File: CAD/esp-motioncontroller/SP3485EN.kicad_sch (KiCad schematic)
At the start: 54 parts, among them J2 Screw_Terminal_01x10, J3 Screw_Terminal_01x10, J4 Screw_Terminal_01x10, J5 Screw_Terminal_01x03, J6 Screw_Terminal_01x10, J8 Screw_Terminal_01x10, U10 AM26LS31CDR, U11 LTV-817S, U12 LTV-817S, U13 LTV-817S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

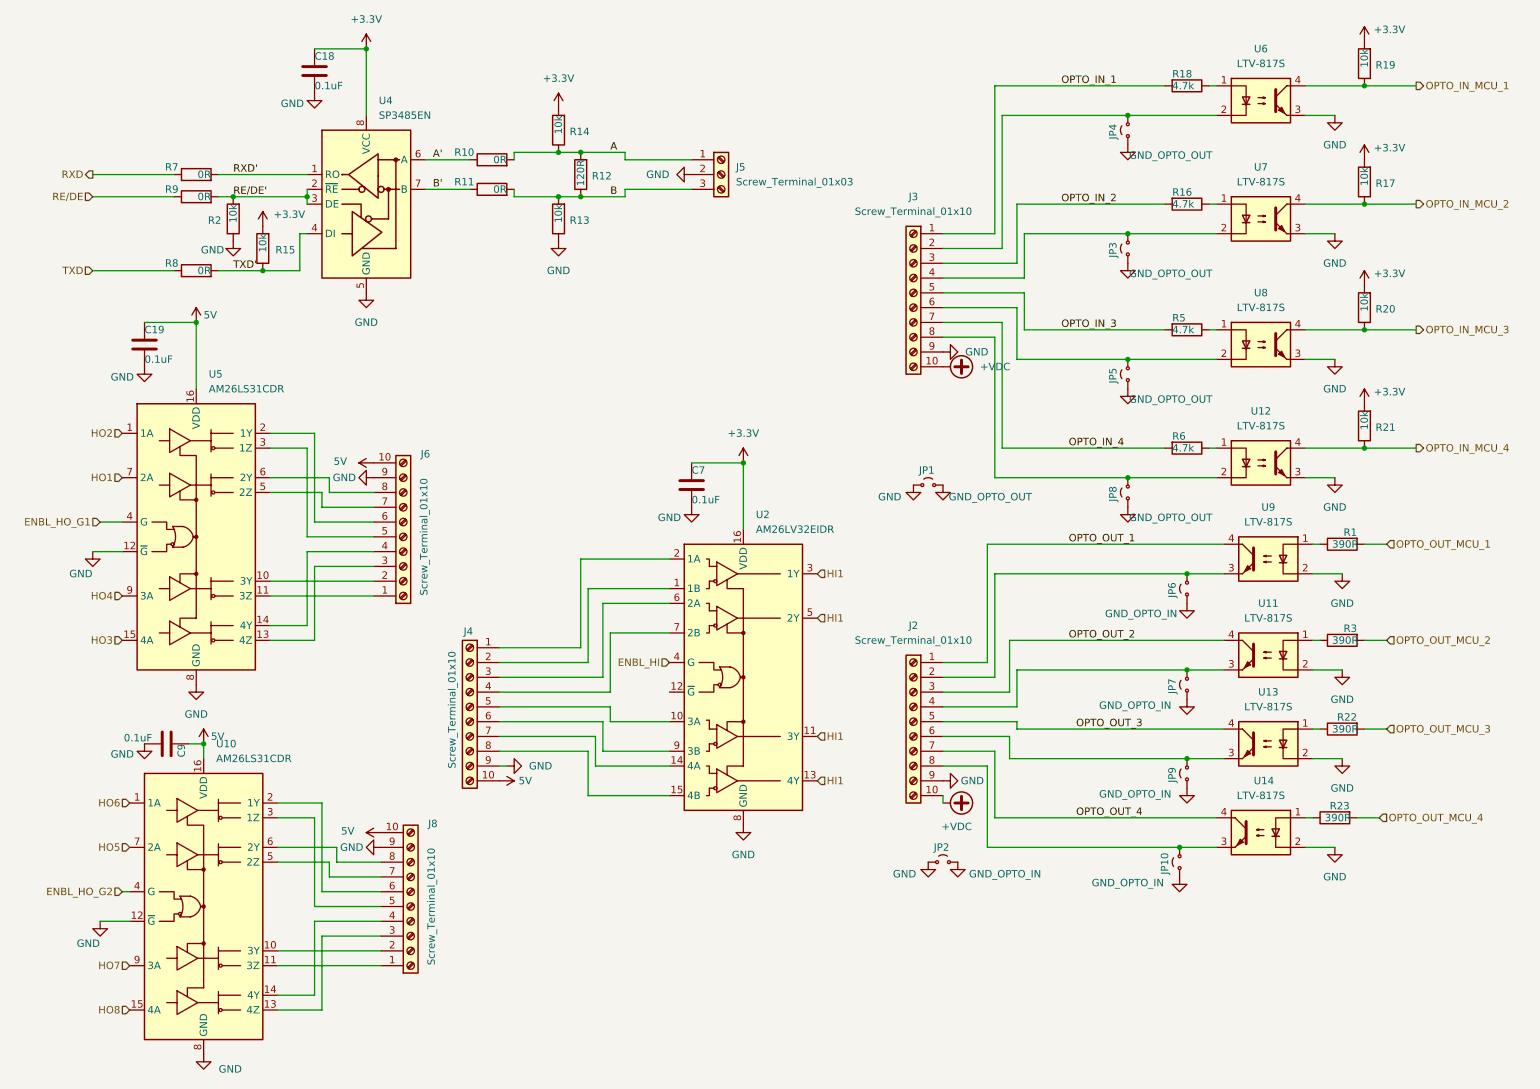
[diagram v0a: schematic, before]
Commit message: Feat: 485 single drivers
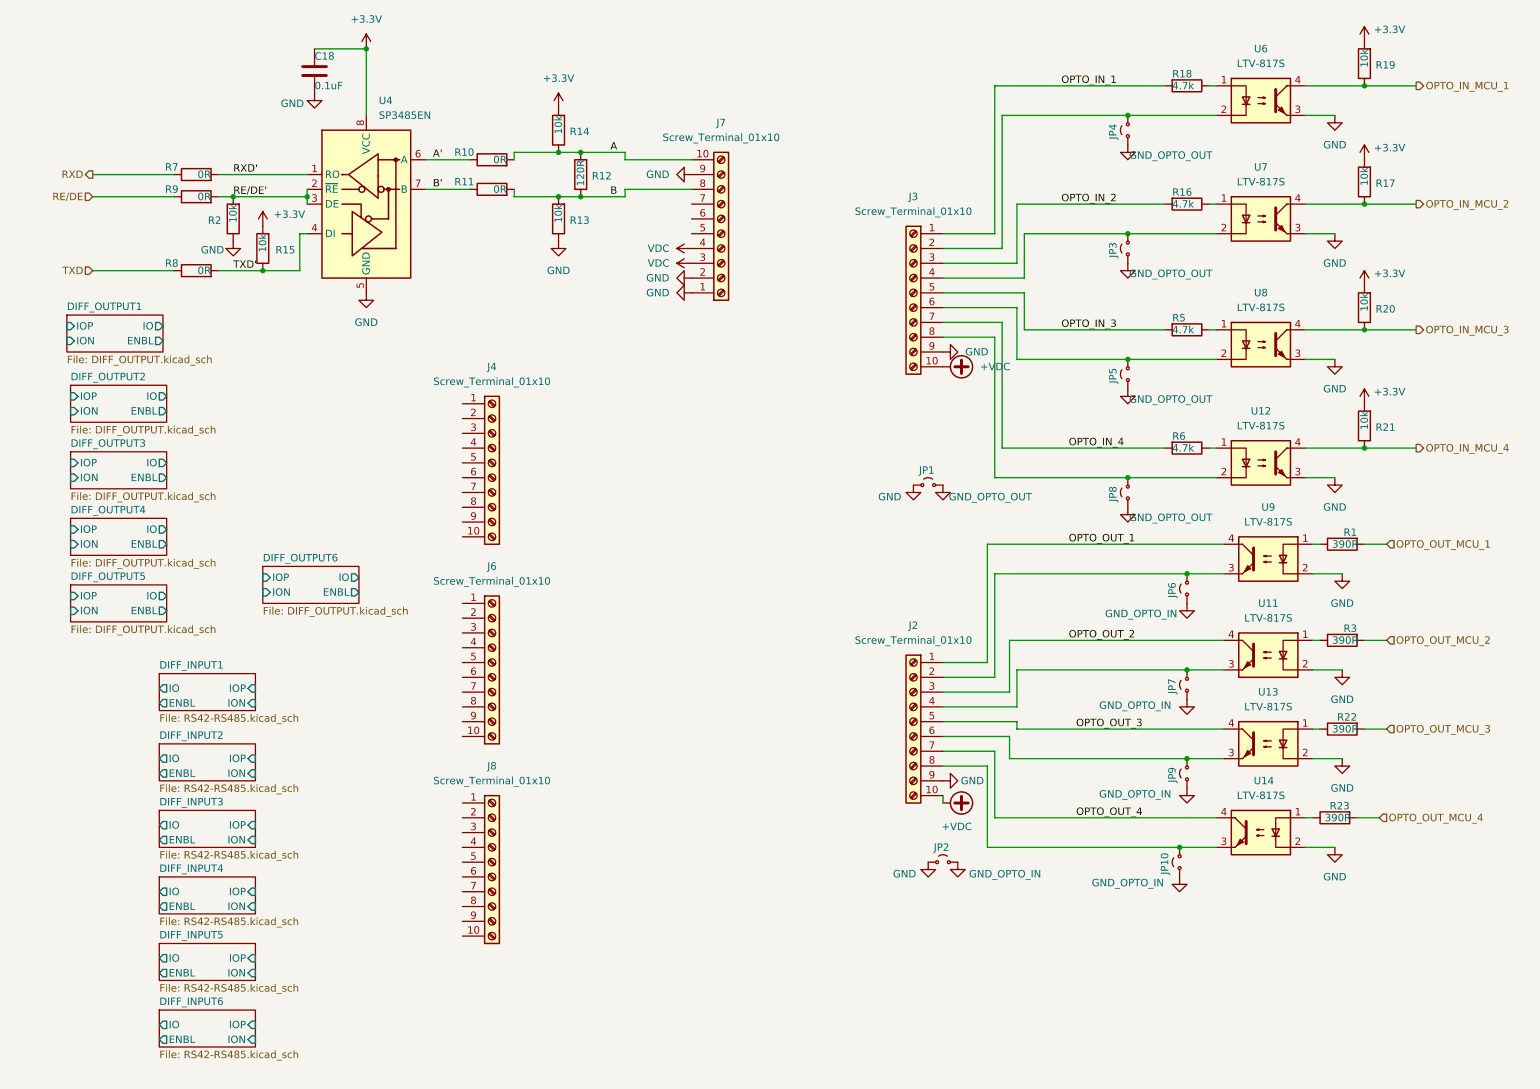
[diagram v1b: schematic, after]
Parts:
- removed C19, C7, C9: 0.1uF, Capacitor_SMD:C_0603_1608Metric, symbol Library:C
- removed J5: Screw_Terminal_01x03, TerminalBlock_Phoenix:TerminalBlock_Phoenix_PT-1,5-3-3.5-H_1x03_P3.50mm_Horizontal, symbol Connector:Screw_Terminal_01x03
- removed U10, U5: AM26LS31CDR, Package_SO:SOIC-16_3.9x9.9mm_P1.27mm, symbol Interface:AM26LS31CD
- removed U2: AM26LV32EIDR, Package_SO:SOIC-16_3.9x9.9mm_P1.27mm, symbol Interface:AM26LV32xD
- added J7: Screw_Terminal_01x10, TerminalBlock_Phoenix:TerminalBlock_Phoenix_PT-1,5-10-3.5-H_1x10_P3.50mm_Horizontal, symbol Connector:Screw_Terminal_01x10
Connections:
- net A: now also J7.10 (Pin_10)
- net B: now also J7.8 (Pin_8)
- net GND: now also J7.1 (Pin_1), J7.2 (Pin_2), J7.9 (Pin_9); no longer J4.9 (Pin_9), J6.9 (Pin_9), J8.9 (Pin_9)
- removed net 5V: J4.10 (Pin_10), J6.10 (Pin_10), J8.10 (Pin_10)
- new net VDC: J7.3 (Pin_3), J7.4 (Pin_4)
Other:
- added sheet DIFF_INPUT1 (RS42-RS485.kicad_sch)
- added sheet DIFF_INPUT2 (RS42-RS485.kicad_sch)
- added sheet DIFF_INPUT3 (RS42-RS485.kicad_sch)
- added sheet DIFF_INPUT4 (RS42-RS485.kicad_sch)
- added sheet DIFF_INPUT5 (RS42-RS485.kicad_sch)
- added sheet DIFF_INPUT6 (RS42-RS485.kicad_sch)
- added sheet DIFF_OUTPUT1 (DIFF_OUTPUT.kicad_sch)
- added sheet DIFF_OUTPUT2 (DIFF_OUTPUT.kicad_sch)
- added sheet DIFF_OUTPUT3 (DIFF_OUTPUT.kicad_sch)
- added sheet DIFF_OUTPUT4 (DIFF_OUTPUT.kicad_sch)
- added sheet DIFF_OUTPUT5 (DIFF_OUTPUT.kicad_sch)
- added sheet DIFF_OUTPUT6 (DIFF_OUTPUT.kicad_sch)

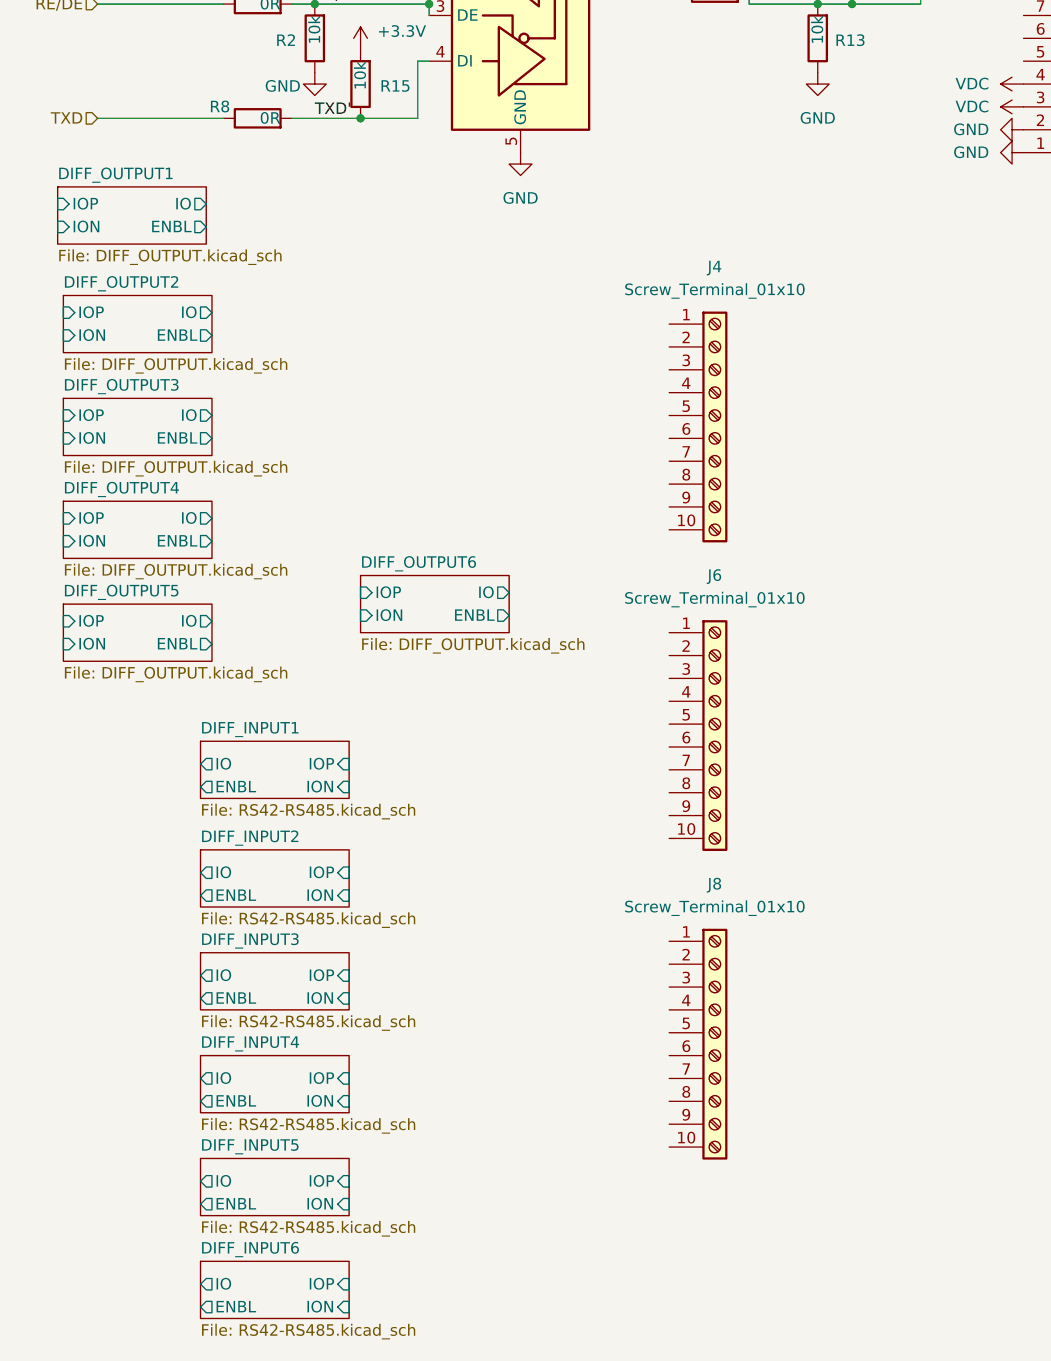
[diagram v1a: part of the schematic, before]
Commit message: Feat: Allmost complete sepdriver
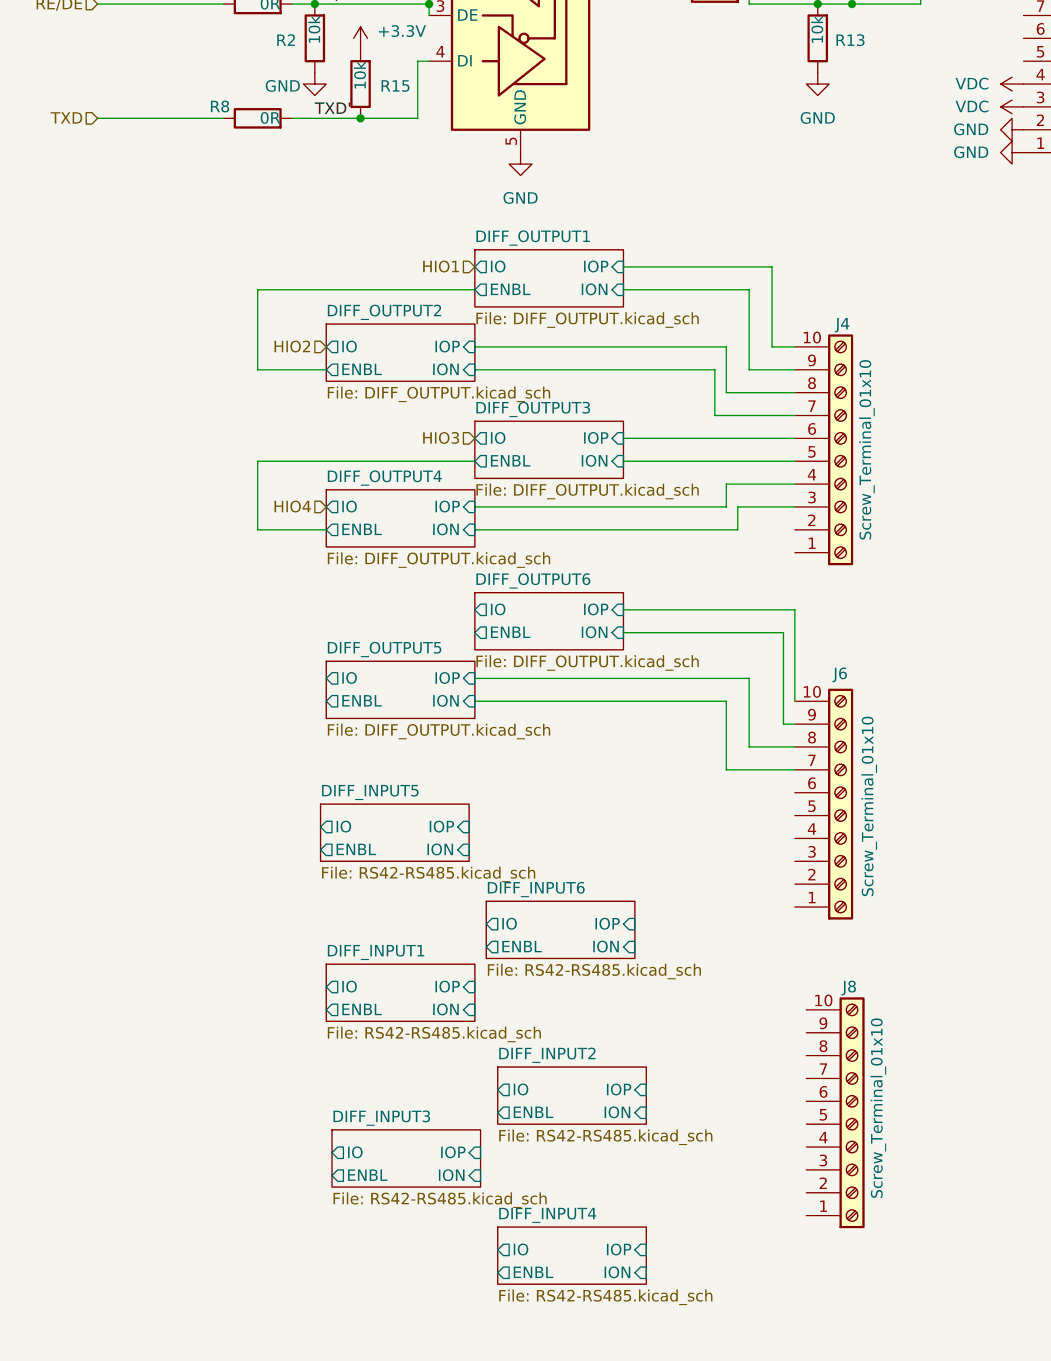
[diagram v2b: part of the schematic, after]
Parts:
- J2, J3, J4, J6, J7, J8: LCSC Part # (none) -> C5184956
- R10, R11, R7, R8, R9: LCSC Part # C17477 -> C21189
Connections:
- net DIFF_OUTPUT1/ION: now also J4.9 (Pin_9)
- net DIFF_OUTPUT1/IOP: now also J4.10 (Pin_10)
- net DIFF_OUTPUT2/ION: now also J4.7 (Pin_7)
- net DIFF_OUTPUT2/IOP: now also J4.8 (Pin_8)
- net DIFF_OUTPUT3/ION: now also J4.5 (Pin_5)
- net DIFF_OUTPUT3/IOP: now also J4.6 (Pin_6)
- net DIFF_OUTPUT4/ION: now also J4.3 (Pin_3)
- net DIFF_OUTPUT4/IOP: now also J4.4 (Pin_4)
- net DIFF_OUTPUT5/ION: now also J6.7 (Pin_7)
- net DIFF_OUTPUT5/IOP: now also J6.8 (Pin_8)
- net DIFF_OUTPUT6/ION: now also J6.9 (Pin_9)
- net DIFF_OUTPUT6/IOP: now also J6.10 (Pin_10)
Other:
- moved on the sheet: J4, J6, J8
